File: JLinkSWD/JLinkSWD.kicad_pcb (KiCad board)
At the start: 2 copper layers, 25.4 x 30.5 mm, 3 parts, among them J1 Conn_01x08, J2 Conn_02x10_Odd_Even, J3 Conn_02x05_Odd_Even

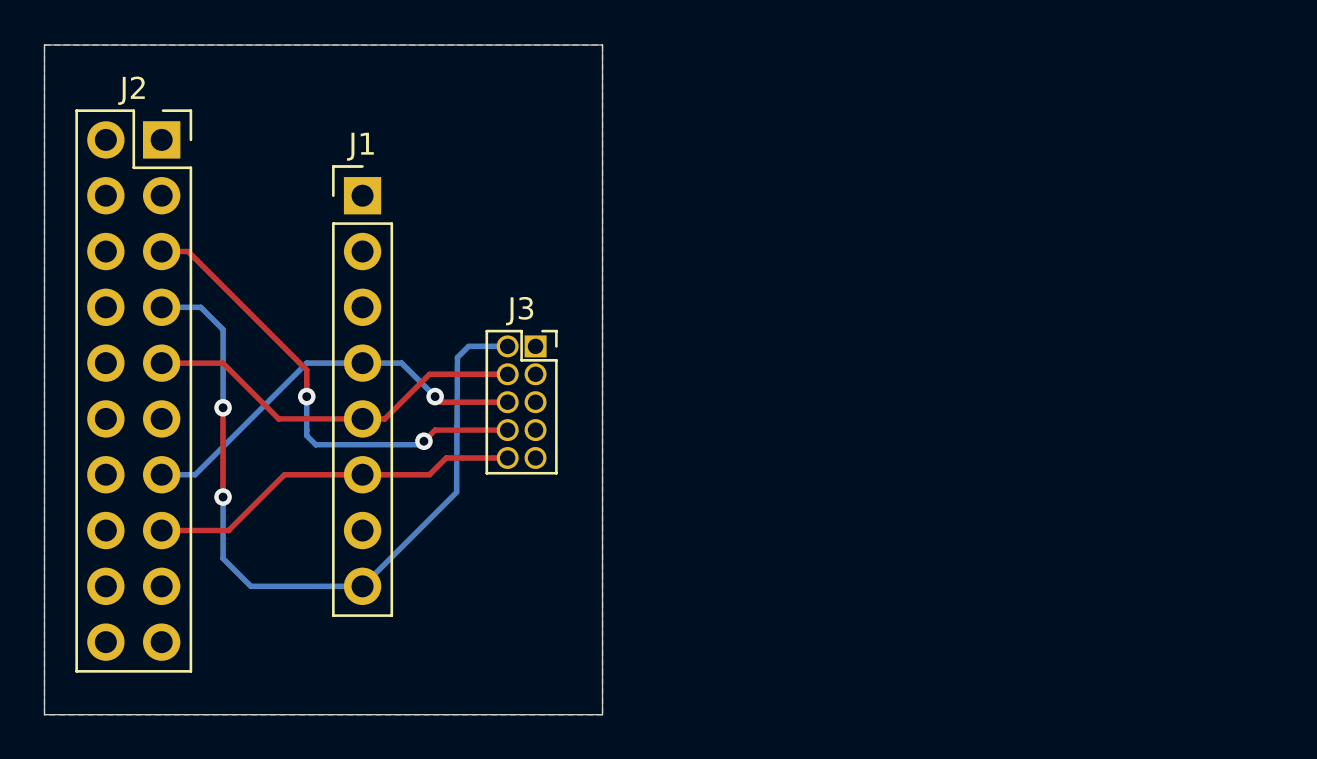
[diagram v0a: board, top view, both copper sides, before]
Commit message: Reduced PCB size
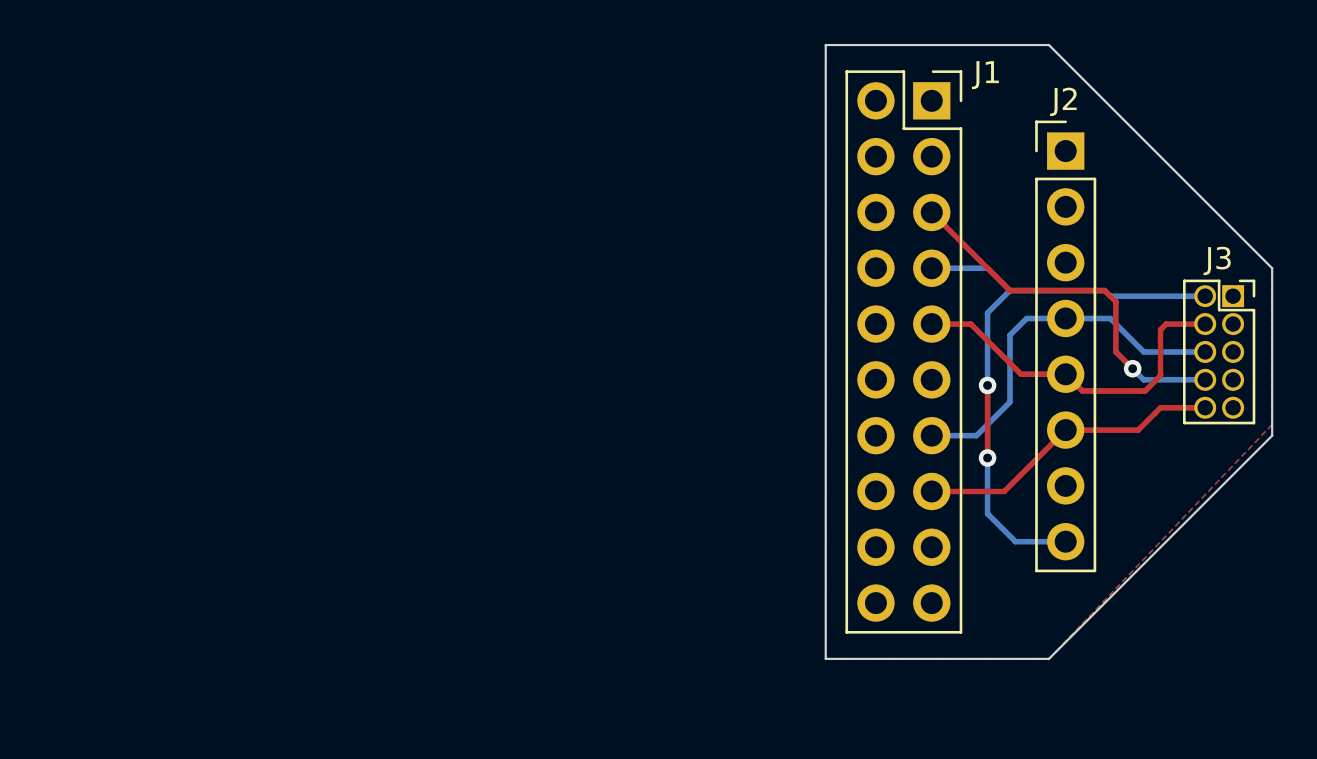
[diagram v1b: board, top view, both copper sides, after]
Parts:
- moved J1 35.1 mm to (167.4, 76.2)
- moved J2 32.1 mm to (173.5, 78.5)
- moved J3 31.8 mm to (181.1, 85.1)
- renumbered J2 to J1, J1 to J2
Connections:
- net Net-(J1-Pad4) renamed /SWD
- net Net-(J1-Pad5) renamed /SWDCLK
- net Net-(J1-Pad6) renamed /RESET
- net Net-(J1-Pad8) renamed /SWDIO
- net Net-(J2-Pad5) renamed /TDI
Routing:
- net /SWDIO: track 35.2 -> 27.6 mm
- net /TDI: track 21.4 -> 17.3 mm, vias 2 -> 1
- net /RESET: track 17.1 -> 14.0 mm
- net /SWD: track 18.6 -> 17.1 mm, vias 1 -> 0
- net /SWDCLK: track 17.6 -> 16.2 mm
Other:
- board size 25.4 x 30.5 mm -> 20.3 x 27.9 mm
